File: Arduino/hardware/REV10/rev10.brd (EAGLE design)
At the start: 88.3 x 55.9 mm, 48 parts, among them IC2 ATMEGA168-AU, Q1 32768Hz, U1 TC1185SMD, U2 ARDUINO

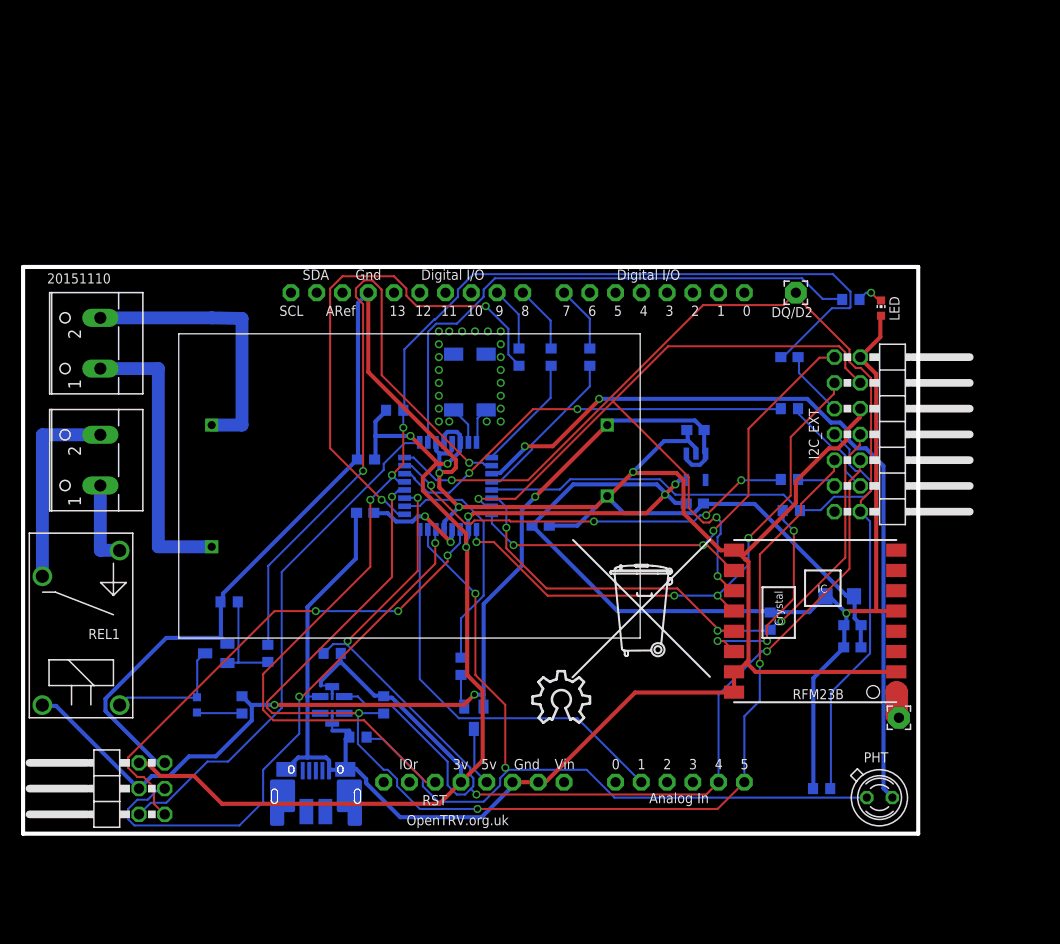
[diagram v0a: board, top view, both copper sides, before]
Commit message: rev10 and 11 updated as per deniz findings
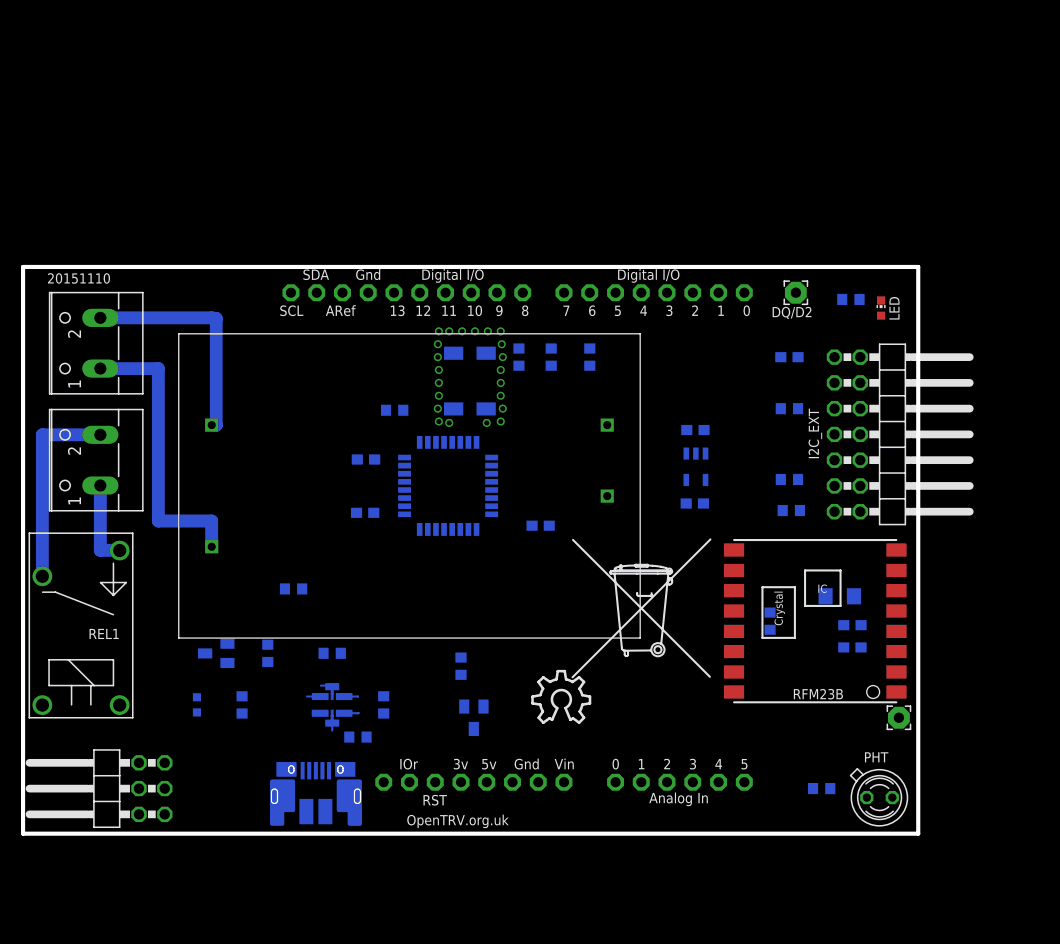
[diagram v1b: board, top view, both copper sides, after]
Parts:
- moved R14 6.48 mm to (26.7, 24.1)
- moved Q1 0.10 mm to (44.1, 44.6)
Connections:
- removed net 5V1: USBPOWER.1
- net 5V: now also USBPOWER.1
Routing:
- net GND: track 324.8 -> 3.70 mm, vias 3 -> 0
- net VCC: track 247.3 -> 2.20 mm, vias 7 -> 0
- net RESET: track 121.5 -> 0.00 mm, vias 3 -> 0
- net SDA: track 122.7 -> 2.05 mm, vias 4 -> 0
- net SCL: track 122.1 -> 2.15 mm, vias 4 -> 0
- net D2: track 102.0 -> 0.00 mm, vias 1 -> 0
- net 5V: track 101.8 -> 0.00 mm, vias 3 -> 0
- net LDR: track 82.6 -> 0.00 mm, vias 2 -> 0
- net IO_POWER_UP: track 78.2 -> 0.00 mm, vias 2 -> 0
- net SPI_MOSI: track 73.3 -> 0.00 mm, vias 3 -> 0
- net BOILER: track 65.5 -> 0.00 mm, vias 2 -> 0
- net SPI_NSS: track 60.4 -> 0.00 mm, vias 3 -> 0
- net SPI_SCK: track 55.3 -> 0.00 mm, vias 4 -> 0
- net LED_HEATCALL_L: track 55.2 -> 0.00 mm
- net N$5: track 54.1 -> 0.00 mm, vias 2 -> 0
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
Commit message: boards routed once again
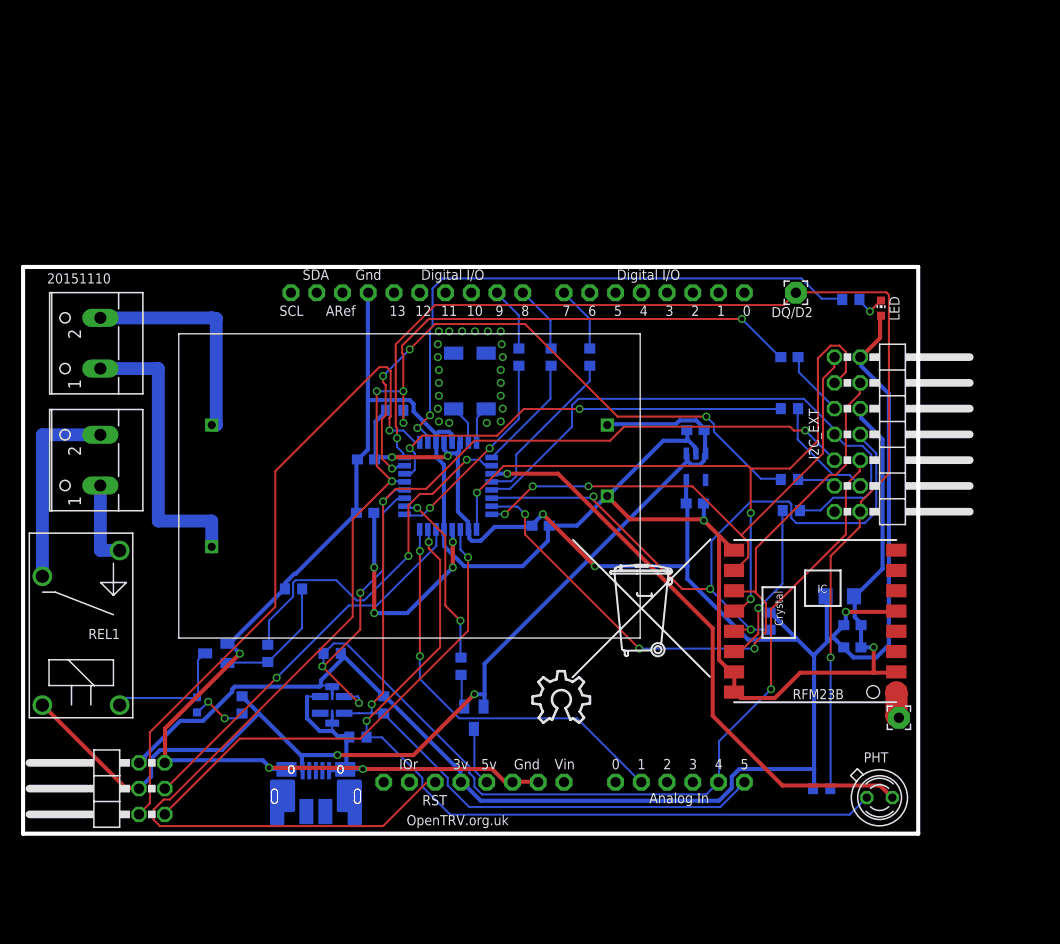
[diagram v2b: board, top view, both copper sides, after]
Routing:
- net GND: track 3.70 -> 249.4 mm, vias 0 -> 5
- net VCC: track 2.20 -> 231.9 mm, vias 0 -> 5
- net RESET: track 0.00 -> 135.7 mm, vias 0 -> 5
- net SCL: track 2.15 -> 118.4 mm, vias 0 -> 3
- net D2: track 0.00 -> 113.6 mm, vias 0 -> 2
- net SDA: track 2.05 -> 114.0 mm, vias 0 -> 4
- net 5V: track 0.00 -> 108.0 mm, vias 0 -> 2
- net LDR: track 0.00 -> 77.7 mm, vias 0 -> 2
- net SPI_SCK: track 0.00 -> 69.8 mm, vias 0 -> 3
- net SPI_NSS: track 0.00 -> 68.1 mm, vias 0 -> 3
- net SPI_MOSI: track 0.00 -> 66.8 mm, vias 0 -> 3
- net VOICE: track 0.00 -> 64.6 mm, vias 0 -> 1
- net RX: track 0.00 -> 59.3 mm, vias 0 -> 4
- net LED_HEATCALL_L: track 0.00 -> 58.1 mm, vias 0 -> 2
- net IO_POWER_UP: track 0.00 -> 57.8 mm, vias 0 -> 1
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
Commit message: rev10 with ground plane
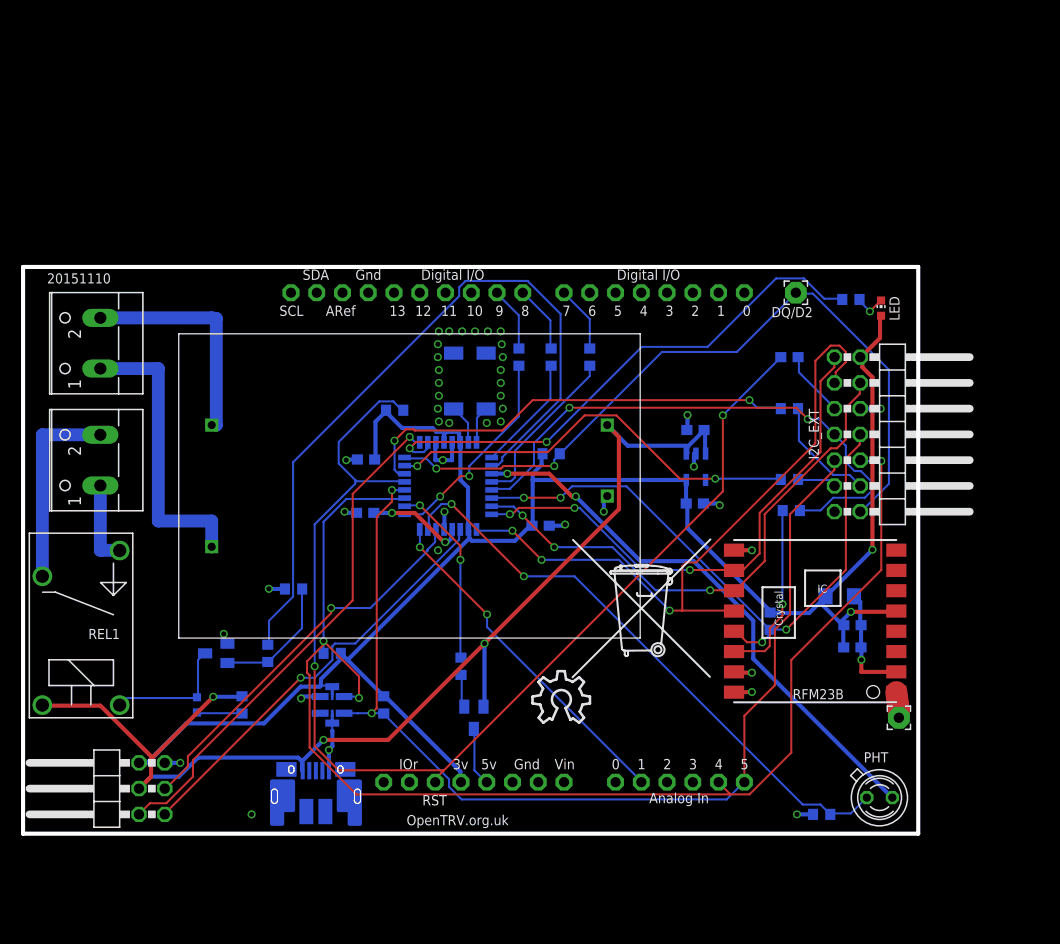
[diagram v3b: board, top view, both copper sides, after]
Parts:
- moved R6 46.4 mm to (78.7, 1.91)
- moved R9 42.4 mm to (52.1, 37.5)
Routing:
- net GND: track 249.4 -> 51.4 mm, vias 5 -> 44
- net VCC: track 231.9 -> 183.4 mm, vias 5 -> 2
- net D2: track 113.6 -> 74.2 mm
- net BOILER: track 36.6 -> 72.8 mm, vias 2 -> 0
- net RESET: track 135.7 -> 115.4 mm, vias 5 -> 2
- net LDR: track 77.7 -> 58.4 mm
- net RX: track 59.3 -> 41.8 mm, vias 4 -> 2
- net SDA: track 114.0 -> 129.9 mm, vias 4 -> 3
- net VOICE: track 64.6 -> 50.4 mm
- net SCL: track 118.4 -> 104.3 mm, vias 3 -> 2
- net N$6: track 23.3 -> 9.90 mm, vias 4 -> 2
- net SPI_MOSI: track 66.8 -> 53.5 mm
- net 5V: track 108.0 -> 117.3 mm, vias 2 -> 3
- net N$15: track 40.8 -> 34.0 mm
- net SPI_NSS: track 68.1 -> 62.4 mm, vias 3 -> 4
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- added copper zone on layer 1, net GND
- added copper zone on layer 16, net GND

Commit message: correcting rev10 psu mirror problem and size
verified by mark to fit. both surprised on the size of it
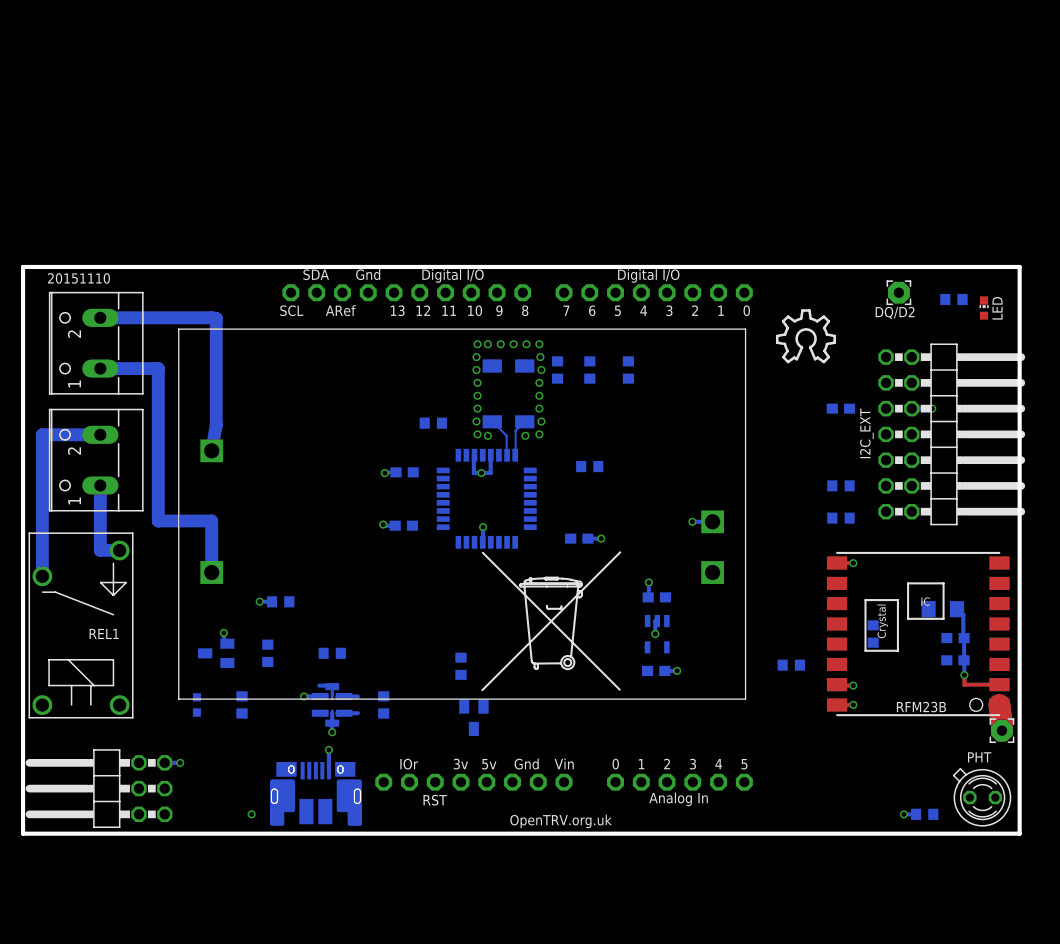
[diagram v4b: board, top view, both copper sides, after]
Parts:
- moved U$1 43.0 mm to (74.4, 46.5)
- moved PSU 29.0 mm to (15.2, 16.5)
- moved C1 16.9 mm to (62.5, 23.3)
- moved C2 16.9 mm to (62.4, 16.0)
- moved U1 16.9 mm to (62.5, 19.7)
- moved R10 15.2 mm to (75.8, 16.6)
- moved C8 10.2 mm to (90.7, 22.1)
- moved ANT1 10.2 mm to (96.5, 10.2)
- moved C4 10.2 mm to (91.9, 19.3)
- moved C7 10.2 mm to (91.9, 17.1)
- moved R12 10.2 mm to (83.8, 19.7)
- moved RFM23B 10.2 mm to (88.3, 19.7)
- moved LED 10.2 mm to (94.8, 51.8)
- moved R6 10.2 mm to (88.9, 1.91)
- moved DQ/D2 10.2 mm to (86.4, 53.3)
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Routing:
- net VCC: track 183.4 -> 2.83 mm, vias 2 -> 0
- net SDA: track 129.9 -> 2.04 mm, vias 3 -> 0
- net 5V: track 117.3 -> 0.10 mm, vias 3 -> 0
- net RESET: track 115.4 -> 0.00 mm, vias 2 -> 0
- net SCL: track 104.3 -> 2.16 mm, vias 2 -> 0
- net D2: track 74.2 -> 0.09 mm, vias 2 -> 0
- net BOILER: track 72.8 -> 0.00 mm
- net SPI_SCK: track 66.8 -> 0.00 mm, vias 3 -> 0
- net SPI_NSS: track 62.4 -> 0.00 mm, vias 4 -> 0
- net LDR: track 58.4 -> 0.00 mm, vias 2 -> 0
- net IO_POWER_UP: track 54.9 -> 0.00 mm, vias 2 -> 0
- net RFM_IRQ: track 54.8 -> 0.00 mm, vias 2 -> 0
- net SPI_MOSI: track 53.5 -> 0.00 mm, vias 3 -> 0
- net LED_HEATCALL_L: track 53.1 -> 0.00 mm, vias 2 -> 0
- net SPI_MISO: track 52.4 -> 0.00 mm, vias 3 -> 0
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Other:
- board size 88.3 x 55.9 mm -> 98.3 x 55.9 mm

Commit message: rev10 reworked as per marks instruction. Almost ready for eyeball
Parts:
- removed DQ/D2: (no value), wirepad:2,15/1,0
- added DQ: (no value), wirepad:2,15/1,0
- I2C_EXT: device pinhead:2X07/90 -> pinhead:2X07
- JP2: device pinhead:2X03/90 -> pinhead:2X03
- moved U2 85.1 mm to (101.6, -2.08), turned to 90 degrees
- moved REL1 81.5 mm to (55.9, 79.4), turned to 180 degrees
- moved I2C_EXT 80.9 mm to (17.8, 5.90), turned to 180 degrees
- moved LED1 76.6 mm to (59.1, 76.8), flipped to the top
- moved R11 69.4 mm to (59.1, 71.1), flipped to the top, turned to 270 degrees
- moved ANT1 68.1 mm to (86.4, 77.5), turned to 0 degrees
- moved U$1 61.3 mm to (14.7, 32.5)
- moved C8 60.1 mm to (65.5, 76.7), flipped to the top, turned to 270 degrees
- moved USBPOWER 59.1 mm to (90.5, 3.70)
- moved C4 57.5 mm to (65.5, 70.3), flipped to the top, turned to 270 degrees
- moved C7 54.1 mm to (65.5, 64.3), flipped to the top, turned to 270 degrees
- moved PSU 53.4 mm to (3.31, 68.6), turned to 270 degrees
- moved RFM23B 50.8 mm to (76.8, 69.2), turned to 270 degrees
- moved PFET 49.0 mm to (90.8, 27.3), flipped to the top, turned to 270 degrees
- moved T1 47.7 mm to (41.9, 59.7), flipped to the top
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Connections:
- removed net N$24: REL1.S, X3.1
- new net N$21: REL1.C, X3.1
- net D2: now also DQ.1; no longer DQ/D2.1
- net N$22: now also REL1.S; no longer REL1.C
- net N$4: now also X1.1; no longer X1.2
- net N$8: now also X1.2; no longer X1.1
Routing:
- net N$8: track 31.1 -> 19.8 mm
- net N$21: track 0.00 -> 10.9 mm
- net N$24: track 8.31 -> 0.00 mm
- net XTAL2: track 3.70 -> 6.24 mm
- net SDA: track 2.04 -> 4.58 mm
- net XTAL1: track 3.92 -> 6.46 mm
- net SCL: track 2.16 -> 4.58 mm
- net N$4: track 24.5 -> 26.8 mm
- net VCC: track 2.83 -> 4.73 mm
- net GND: track 47.5 -> 48.6 mm
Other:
- board size 98.3 x 55.9 mm -> 100 x 80 mm
- board text added: "5V"
- board text added: "A6"
- board text added: "A7"
- board text added: "DQ"
- board text added: "GND"
- board text added: "IRQ"
- board text added: "Mi"
- board text added: "Miso"
- board text added: "Mo"
- board text added: "Mosi"
- board text added: "NSS"
- board text added: "RST"
- board text added: "RX"
- board text added: "SCK"
- board text added: "SCL"
- board text added: "SDA"
- board text added: "TX"
- board text added: "VCC"
- board text added: "VOICE"

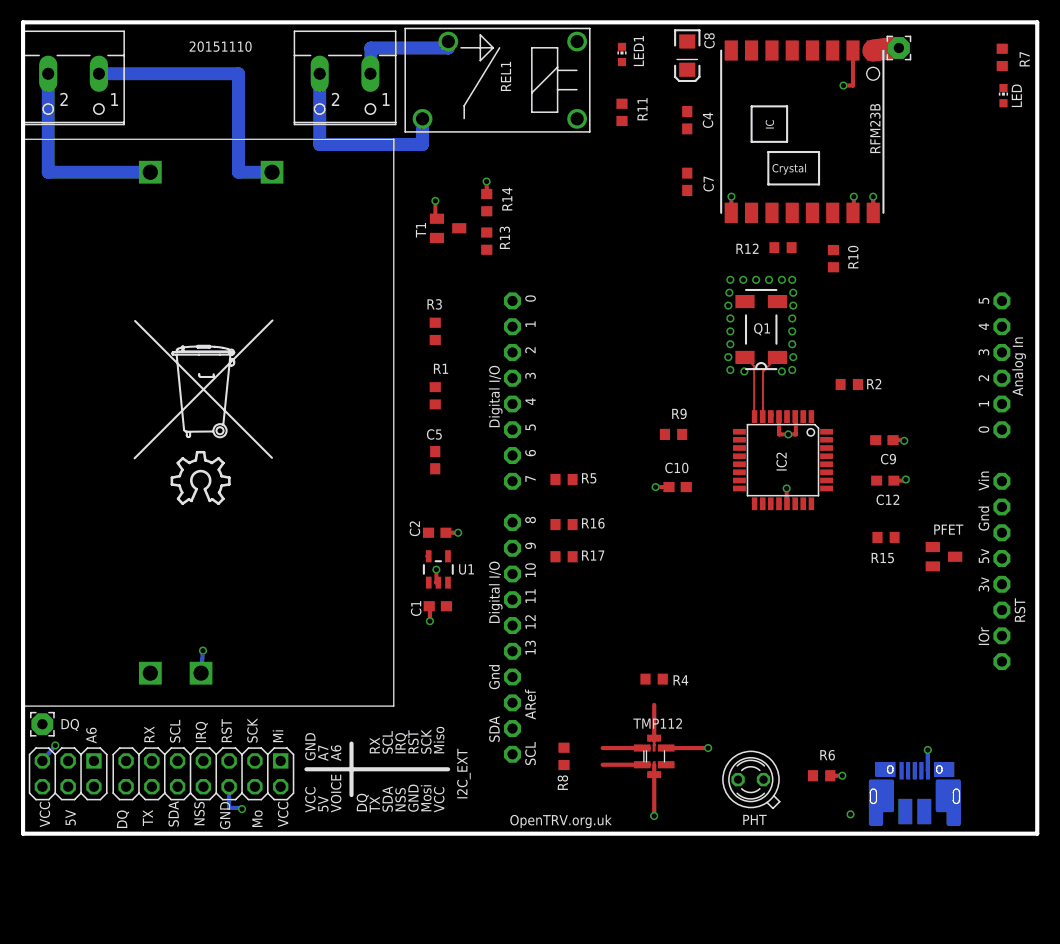
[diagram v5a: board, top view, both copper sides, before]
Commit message: more corrections to rev10
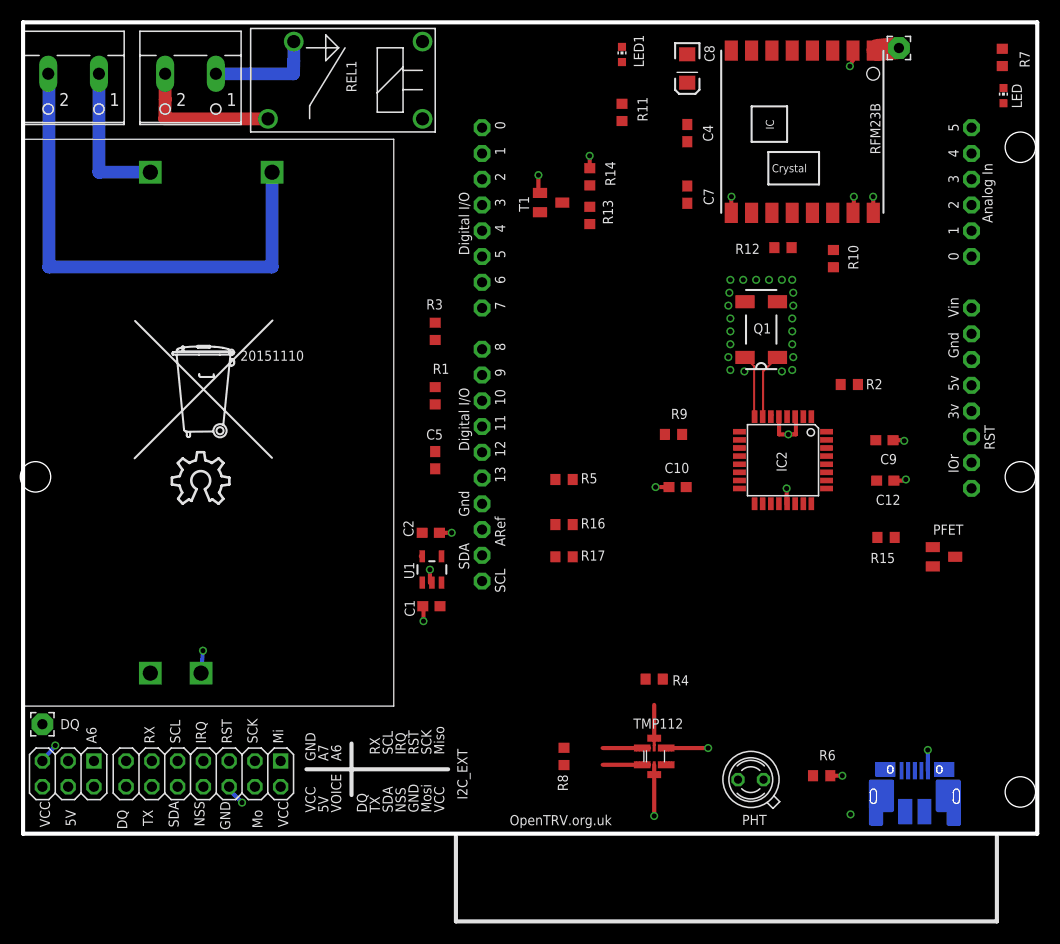
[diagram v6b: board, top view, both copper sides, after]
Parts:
- moved U2 17.3 mm to (98.6, 15.0)
- moved REL1 15.2 mm to (40.6, 79.4)
- moved X3 15.2 mm to (16.5, 73.7)
- moved R13 10.5 mm to (55.9, 61.0)
- moved R14 10.5 mm to (55.9, 64.8)
- moved T1 10.5 mm to (52.1, 62.2)
- moved C8 1.27 mm to (65.5, 75.4)
- moved C4 1.27 mm to (65.5, 69.1)
- moved C7 1.27 mm to (65.5, 63.0)
- moved C1 0.63 mm to (40.3, 22.4)
- moved C2 0.63 mm to (40.2, 29.7)
- moved U1 0.63 mm to (40.3, 26.1)
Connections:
- net N$4: now also X1.2; no longer X1.1
- net N$8: now also X1.1; no longer X1.2
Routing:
- net N$4: track 26.8 -> 50.5 mm
- net N$22: track 19.7 -> 14.6 mm
- net N$8: track 19.8 -> 14.8 mm
- net GND: track 48.6 -> 44.4 mm
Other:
- board text added: "Seal off solderpads with hotmelt glue or silicone glue"
- board text removed: "Seal of solderpads with hotmelt glue or silicone glue"
